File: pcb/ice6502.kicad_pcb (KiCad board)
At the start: 2 copper layers, 100 x 50 mm, 54 parts, among them J1 Programming Header, J2 RDY, J3 RESB, J4 VIN, J5 GND, J6 3v3, J7 1v2, J8 GND, U0 iCE40-HX4K-TQ144, U1 AT25SF041-SSHD-B, U1_1 W65C816S_PLCC, U2 VXO7803-1000, U3 IS61WV5128EDBLL-10TLI, X1 ASE-xxxMHz

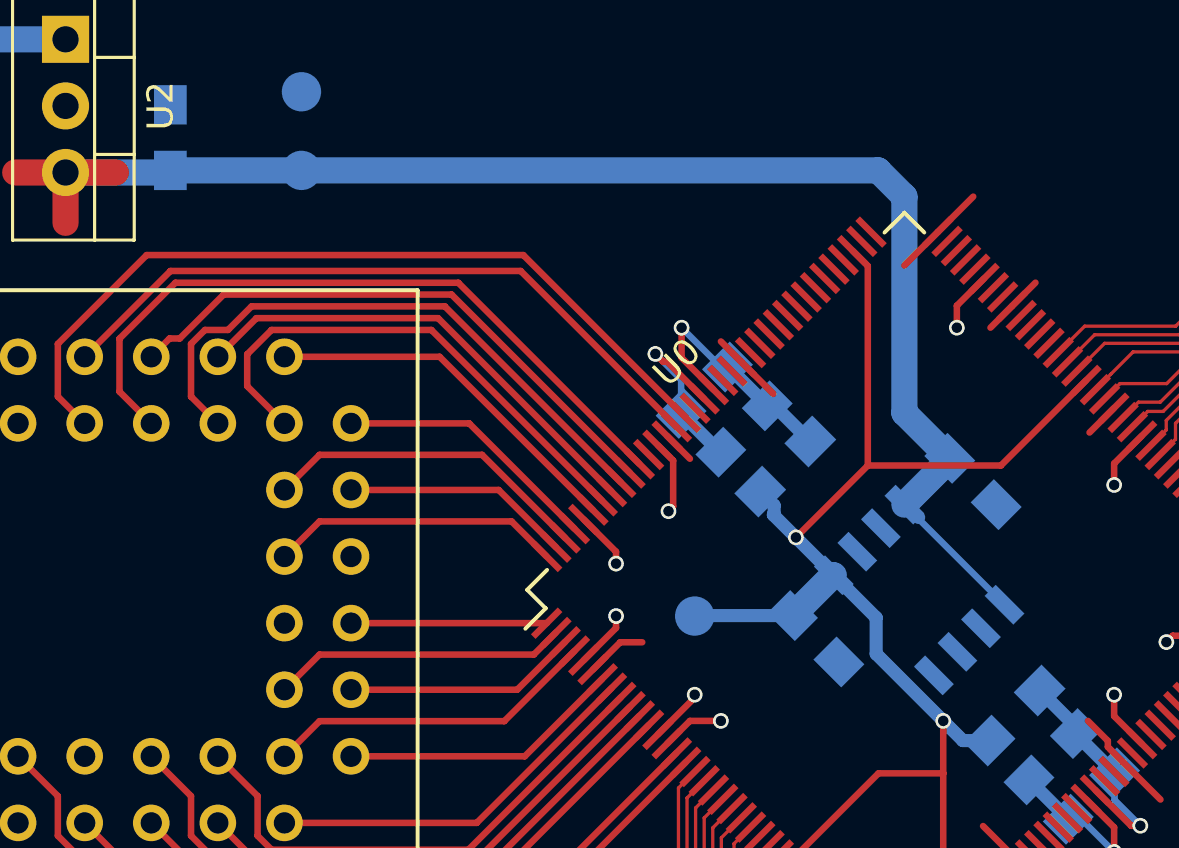
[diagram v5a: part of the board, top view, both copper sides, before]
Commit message: Align more components on grid
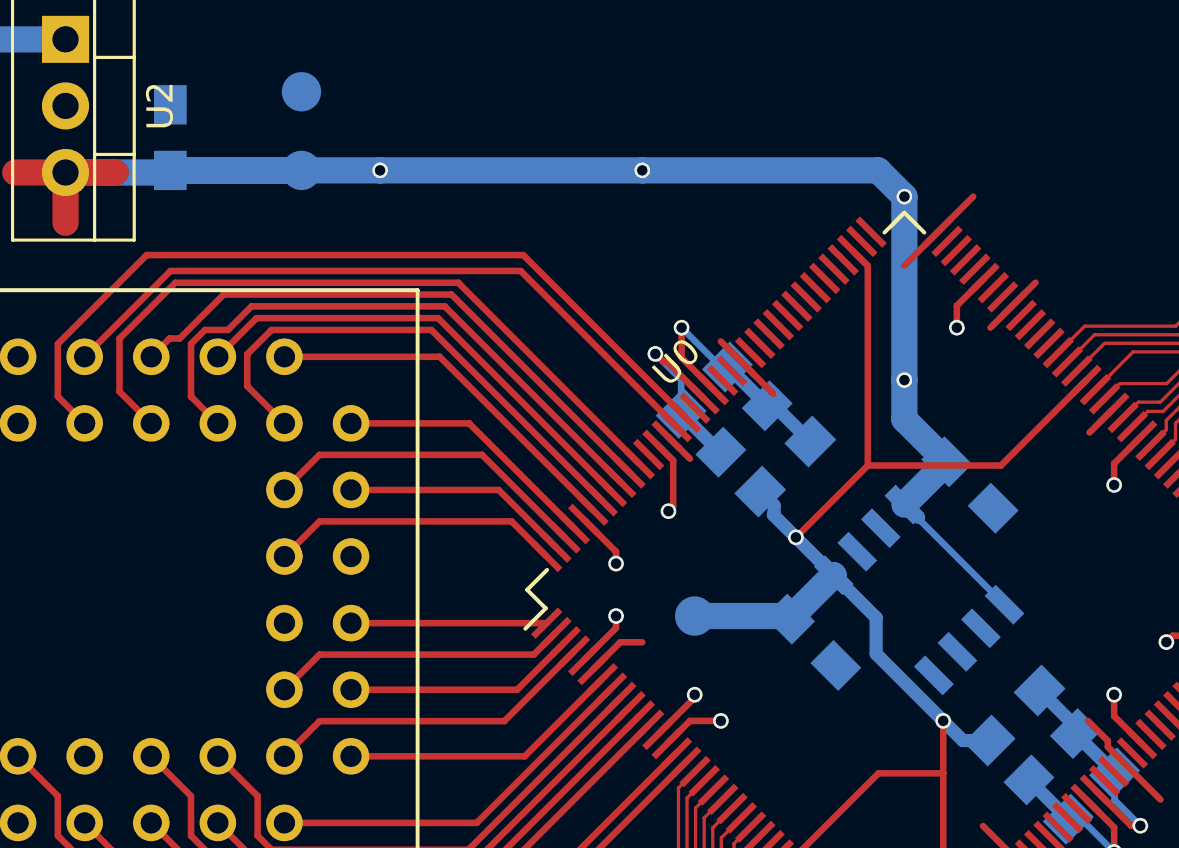
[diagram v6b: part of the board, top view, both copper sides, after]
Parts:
- moved C10 0.18 mm to (96.5, 77.0)
- moved C9 0.18 mm to (102.5, 71.0)
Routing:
- net 3v3: track 87.5 -> 92.4 mm, vias 0 -> 4
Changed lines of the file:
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@@
     (thickness 1.6)
     (drawings 4)
-    (tracks 455)
+    (tracks 464)
     (zones 0)
     (modules 54)
@@
   )
   (setup
-    (last_trace_width 0.127)
+    (last_trace_width 1)
     (user_trace_width 0.127)
     (user_trace_width 0.2286)
@@
     (path /top/powerSupply0/reg3v30/11708806798554095915)
     (attr smd)
-    (fp_text reference C8 (at 0 1.75 90) (layer B.SilkS)
+    (fp_text reference C8 (at -3.25 0 90) (layer B.SilkS)
       (effects (font (size 1 1) (thickness 0.15)) (justify mirror))
     )
@@
   )
   (module C_0805_HandSoldering (layer B.Cu)
-    (at 102.616117 70.866117 315)
+    (at 102.5 71 315)
     (descr "Capacitor SMD 0805, hand soldering")
     (tags "capacitor 0805")
     (path /top/powerSupply0/reg1v20/12323081384701485743)
     (attr smd)
-    (fp_text reference C9 (at 3.548096 0.176777 315) (layer B.SilkS)
+    (fp_text reference C9 (at 3.535534 0 315) (layer B.SilkS)
       (effects (font (size 1 1) (thickness 0.15)) (justify mirror))
     )
@@
   )
   (module C_0805_HandSoldering (layer B.Cu)
-    (at 96.616117 76.866117 315)
+    (at 96.5 77 315)
     (descr "Capacitor SMD 0805, hand soldering")
     (tags "capacitor 0805")
     (path /top/powerSupply0/reg1v20/18175665618970243292)
     (attr smd)
-    (fp_text reference C10 (at 0.012562 1.59099 315) (layer B.SilkS)
+    (fp_text reference C10 (at 0 2.12132 315) (layer B.SilkS)
       (effects (font (size 1 1) (thickness 0.15)) (justify mirror))
     )
@@
     (path /top/powerSupply0/testPoint2/868412879809708017)
     (attr virtual)
-    (fp_text reference J6 (at 0 1.648) (layer B.SilkS)
-      (effects (font (size 1 1) (thickness 0.15)) (justify mirror))
-    )
-    (fp_text value 3v3 (at 0 -1.75) (layer B.Fab)
+    (fp_text reference J6 (at 0 1.648) (layer B.Fab)
+      (effects (font (size 1 1) (thickness 0.15)) (justify mirror))
+    )
+    (fp_text value 3v3 (at -2.5 0) (layer B.SilkS)
       (effects (font (size 1 1) (thickness 0.15)) (justify mirror))
     )
@@
     (path /top/powerSupply0/testPoint3/8356988870729559571)
     (attr virtual)
-    (fp_text reference J7 (at 0 1.648) (layer B.SilkS)
-      (effects (font (size 1 1) (thickness 0.15)) (justify mirror))
-    )
-    (fp_text value 1v2 (at 0 -1.75) (layer B.Fab)
+    (fp_text reference J7 (at 0 2) (layer B.Fab)
+      (effects (font (size 1 1) (thickness 0.15)) (justify mirror))
+    )
+    (fp_text value 1v2 (at 0 1.5) (layer B.SilkS)
       (effects (font (size 1 1) (thickness 0.15)) (justify mirror))
     )
@@
     (path /top/powerSupply0/testPoint4/10497025430823907841)
     (attr virtual)
-    (fp_text reference J8 (at 0 1.648) (layer B.SilkS)
-      (effects (font (size 1 1) (thickness 0.15)) (justify mirror))
-    )
-    (fp_text value GND (at 0 -1.75) (layer B.Fab)
+    (fp_text reference J8 (at 0 1.648) (layer B.Fab)
+      (effects (font (size 1 1) (thickness 0.15)) (justify mirror))
+    )
+    (fp_text value GND (at -2.5 0) (layer B.SilkS)
       (effects (font (size 1 1) (thickness 0.15)) (justify mirror))
     )
@@
   (segment (start 93 69.75) (end 92.964468 69.75) (width 0.5) (layer B.Cu) (net 65) (status 30))
   (segment (start 92.964468 69.75) (end 91.482234 68.267766) (width 0.5) (layer B.Cu) (net 65) (status 30))
+  (segment (start 101.616117 70.116117) (end 101.616117 70.133883) (width 1) (layer B.Cu) (net 66))
+  (segment (start 101.616117 70.133883) (end 100 71.75) (width 1) (layer B.Cu) (net 66))
+  (segment (start 100 67) (end 100 68.5) (width 1) (layer B.Cu) (net 66))
+  (segment (start 100 68.5) (end 101.616117 70.116117) (width 1) (layer B.Cu) (net 66))
+  (via (at 80 59) (size 0.6) (drill 0.4) (layers F.Cu B.Cu) (net 66))
+  (segment (start 72 59) (end 77 59) (width 1) (layer B.Cu) (net 66))
+  (segment (start 100 60) (end 100 67) (width 1) (layer B.Cu) (net 66))
+  (via (at 100 67) (size 0.6) (drill 0.4) (layers F.Cu B.Cu) (net 66))
+  (via (at 100 60) (size 0.6) (drill 0.4) (layers F.Cu B.Cu) (net 66))
+  (segment (start 90 59) (end 99 59) (width 1) (layer B.Cu) (net 66))
+  (segment (start 80 59) (end 90 59) (width 1) (layer B.Cu) (net 66))
+  (via (at 90 59) (size 0.6) (drill 0.4) (layers F.Cu B.Cu) (net 66))
+  (segment (start 72 59) (end 80 59) (width 1) (layer B.Cu) (net 66))
   (segment (start 113.647161 76.272792) (end 114.75 77.375631) (width 0.25) (layer F.Cu) (net 66) (status 10))
   (segment (start 99 59) (end 100 60) (width 1) (layer B.Cu) (net 66))
-  (segment (start 100 60) (end 100 68.25) (width 1) (layer B.Cu) (net 66))
-  (segment (start 72 59) (end 99 59) (width 1) (layer B.Cu) (net 66) (status 10))
-  (segment (start 100 68.25) (end 101.732234 69.982234) (width 1) (layer B.Cu) (net 66) (status 20))
   (segment (start 93.77746 66.302587) (end 95 67.525127) (width 0.25) (layer F.Cu) (net 66) (status 10))
   (segment (start 90.949033 69.131014) (end 91.818019 70) (width 0.25) (layer F.Cu) (net 66) (status 10))
@@
   (segment (start 100 71.75) (end 103.818377 75.568377) (width 0.25) (layer B.Cu) (net 66) (status 30))
   (segment (start 104.454773 85.454773) (end 104.454773 85.46518) (width 0.25) (layer F.Cu) (net 66) (status 30))
-  (segment (start 101.732234 69.982234) (end 101.732234 70.017766) (width 1) (layer B.Cu) (net 66) (status 30))
-  (segment (start 101.732234 70.017766) (end 100 71.75) (width 1) (layer B.Cu) (net 66) (status 30))
   (segment (start 131.7 78.55) (end 131.5 78.75) (width 0.5) (layer B.Cu) (net 66) (status 30))
   (segment (start 100.543773 72.23785) (end 100 71.694077) (width 0.5) (layer B.Cu) (net 66) (status 30))
@@
   (segment (start 112.586501 77.333452) (end 112.583452 77.333452) (width 0.25) (layer F.Cu) (net 67) (status 30))
   (segment (start 131 81.75) (end 131.5 81.25) (width 0.5) (layer B.Cu) (net 67) (status 30))
-  (segment (start 95.732234 75.982234) (end 92.017766 75.982234) (width 0.5) (layer B.Cu) (net 68) (status 30))
+  (segment (start 92 76) (end 95.5 76) (width 1) (layer B.Cu) (net 68))
+  (segment (start 95.5 76) (end 95.616117 76.116117) (width 1) (layer B.Cu) (net 68))
+  (segment (start 97.305923 74.444077) (end 97.288157 74.444077) (width 1) (layer B.Cu) (net 68))
+  (segment (start 97.288157 74.444077) (end 95.616117 76.116117) (width 1) (layer B.Cu) (net 68))
   (segment (start 92.017766 75.982234) (end 92 76) (width 0.5) (layer B.Cu) (net 68) (status 30))
   (segment (start 101.480762 82) (end 101.480762 86.733811) (width 0.25) (layer F.Cu) (net 68))
@@
   (segment (start 102.230762 80.75) (end 103.25 80.75) (width 0.5) (layer B.Cu) (net 68) (status 20))
   (segment (start 94.5 71.638154) (end 94.5 71.25) (width 0.25) (layer B.Cu) (net 68) (status 30))
-  (segment (start 97.305923 74.444077) (end 97.270391 74.444077) (width 1) (layer B.Cu) (net 68) (status 30))
-  (segment (start 97.270391 74.444077) (end 95.732234 75.982234) (width 1) (layer B.Cu) (net 68) (status 30))
   (segment (start 102.333452 87.583452) (end 102.333452 87.586501) (width 0.25) (layer F.Cu) (net 68) (status 30))
   (segment (start 96 95.5) (end 96 96.85) (width 0.25) (layer B.Cu) (net 69) (status 20))

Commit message: wip
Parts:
- J2, J3: moved to B.Cu
- moved R17 1.41 mm to (54.5, 73.5), turned to 0 degrees
- moved R16 1.33 mm to (54.5, 76.5), turned to 0 degrees
- moved R3 0.29 mm to (104.0, 80.0)
- moved R4 0.21 mm to (95.5, 70.5)
- moved C1 0.19 mm to (105.5, 81.5)
- moved C2 0.19 mm to (107.0, 83.0)
- moved C3 0.18 mm to (92.5, 67.5)
- moved C4 0.18 mm to (94.0, 69.0)
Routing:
- net N$28: track 11.3 -> 0.38 mm
- net N$29: track 7.41 -> 0.16 mm
- net PLLGND_1: track 7.38 -> 6.13 mm
- net PLLVCC: track 9.31 -> 10.3 mm
- net 1v2: track 57.5 -> 56.8 mm
- net PLLVCC_1: track 10.2 -> 9.70 mm

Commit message: Tidying pcb
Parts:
- moved J1 13.4 mm to (139.0, 94.5), turned to 270 degrees
- moved R2 5.64 mm to (114.5, 89.0), turned to 135 degrees
- moved R1 4.18 mm to (116.0, 87.5), turned to 135 degrees
- moved U1 2.24 mm to (119.0, 85.0), turned to 315 degrees
- moved J2 1.00 mm to (56.0, 76.2)
- moved J3 1.00 mm to (56.0, 73.8)
- moved R16 0.25 mm to (54.5, 76.2)
- moved R17 0.25 mm to (54.5, 73.8)
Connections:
- net N$28 renamed RDY
- net N$29 renamed RESB
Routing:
- net RDY: track 0.38 -> 17.9 mm
- net SCK: track 0.00 -> 13.5 mm
- net MOSI: track 0.00 -> 13.5 mm
- net RESB: track 0.16 -> 10.4 mm
- net N$2: track 0.00 -> 9.61 mm
- net MISO: track 0.00 -> 7.36 mm
- net CS: track 0.00 -> 7.26 mm
